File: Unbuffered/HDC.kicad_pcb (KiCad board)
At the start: 2 copper layers, 84.3 x 56.6 mm, 17 parts, among them J1 Spectrum 128/Grey +2 edge con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, J2 HDD_LED, J3 POWER, J4 PATA_40, J5 DOM_POWER_ENABLE, Q1 BC327, U3 74LS10

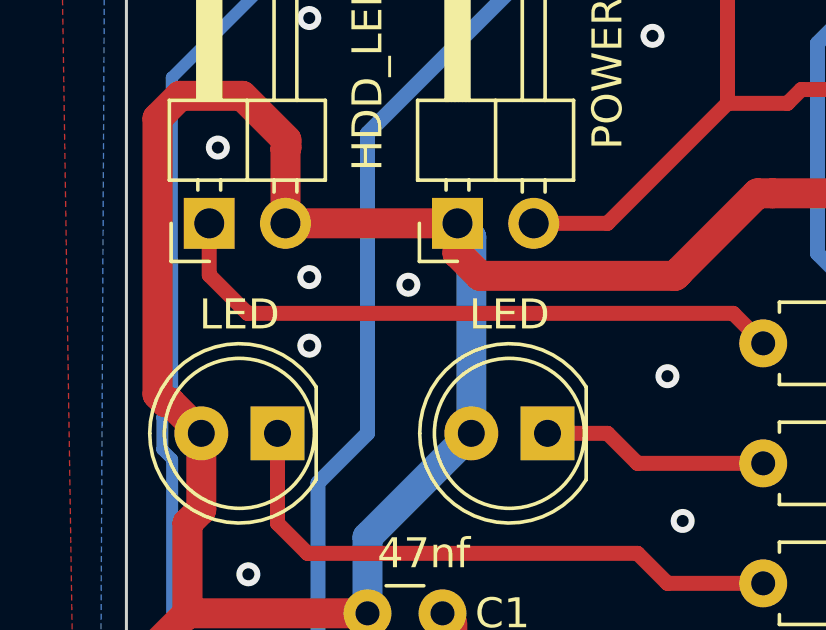
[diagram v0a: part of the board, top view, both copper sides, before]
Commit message: Fixed the silk screen on the buffered version to properly credit the original designers.
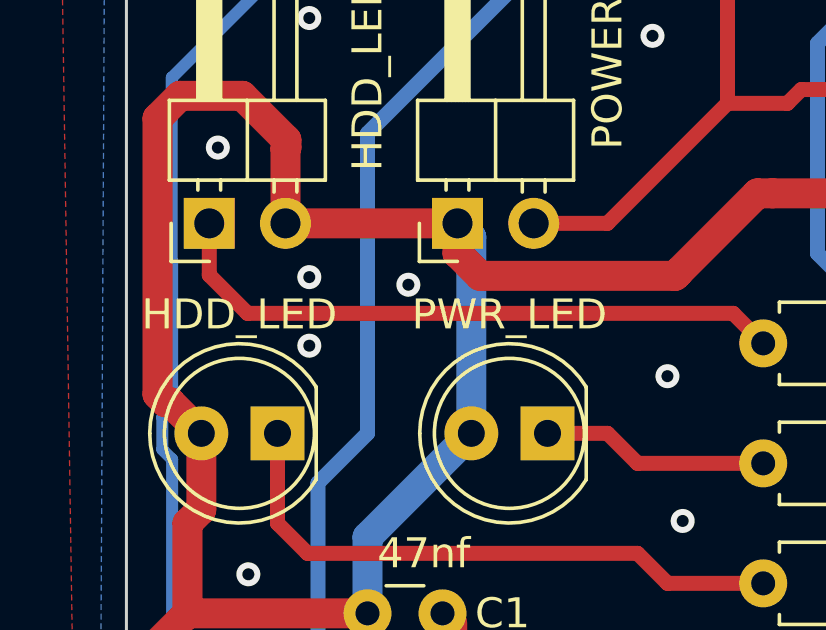
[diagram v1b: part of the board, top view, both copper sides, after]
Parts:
- D1: value LED -> HDD_LED
- D2: value LED -> PWR_LED
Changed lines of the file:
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@@
       (effects (font (size 1 1) (thickness 0.15)))
     )
-    (fp_text value "LED" (at 1.27 3.96) (layer "F.SilkS")
+    (fp_text value "HDD_LED" (at 1.27 3.96) (layer "F.SilkS")
       (effects (font (size 1 1) (thickness 0.15)))
     )
@@
       (effects (font (size 1 1) (thickness 0.15)))
     )
-    (fp_text value "LED" (at 1.27 3.96) (layer "F.SilkS")
-      (effects (font (size 1 1) (thickness 0.15)))
-    )
+    (fp_text value "PWR_LED" (at 1.27 3.96) (layer "F.SilkS")
+      (effects (font (size 1 1) (thickness 0.15)))
+    )
